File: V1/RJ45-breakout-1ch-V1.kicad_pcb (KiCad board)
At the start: 2 copper layers, 22.9 x 30.5 mm, 3 parts, among them J1 RJ45, J2 Screw_Terminal_01x04

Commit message: Footprint updated
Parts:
- removed REF**: OSHW-Logo2_7.3x6mm_Copper, Symbol:OSHW-Logo2_7.3x6mm_Copper

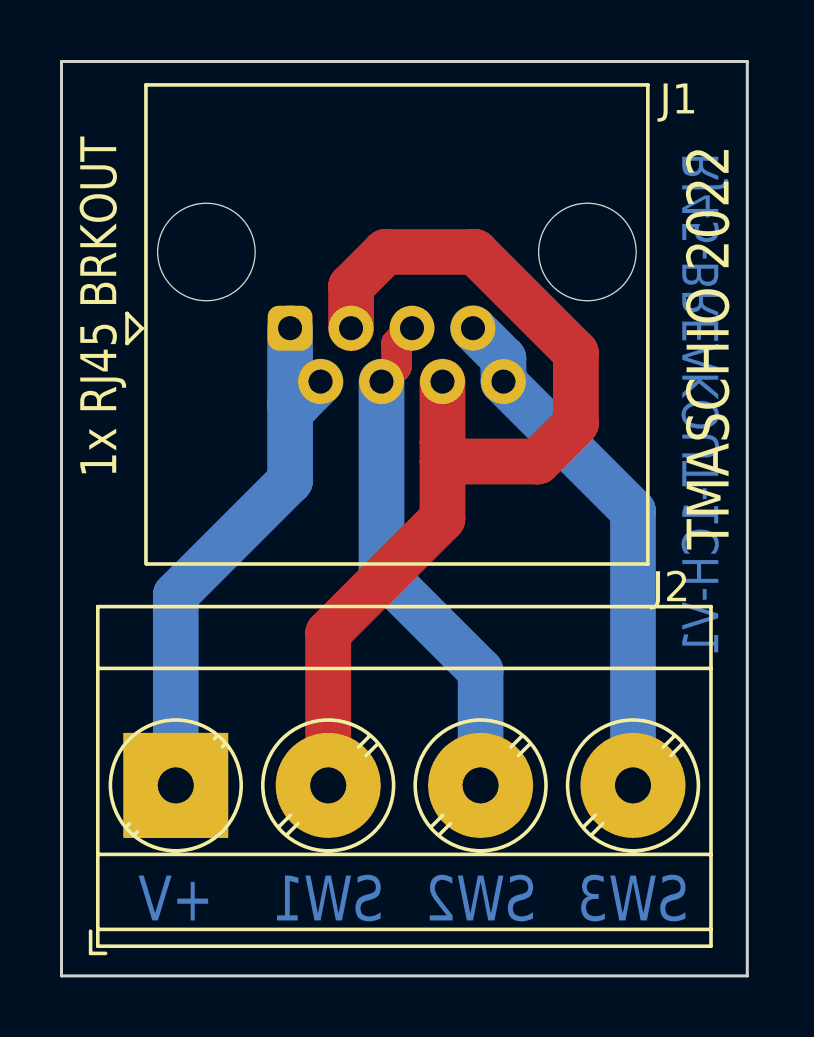
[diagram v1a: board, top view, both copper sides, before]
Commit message: PCB size optimization
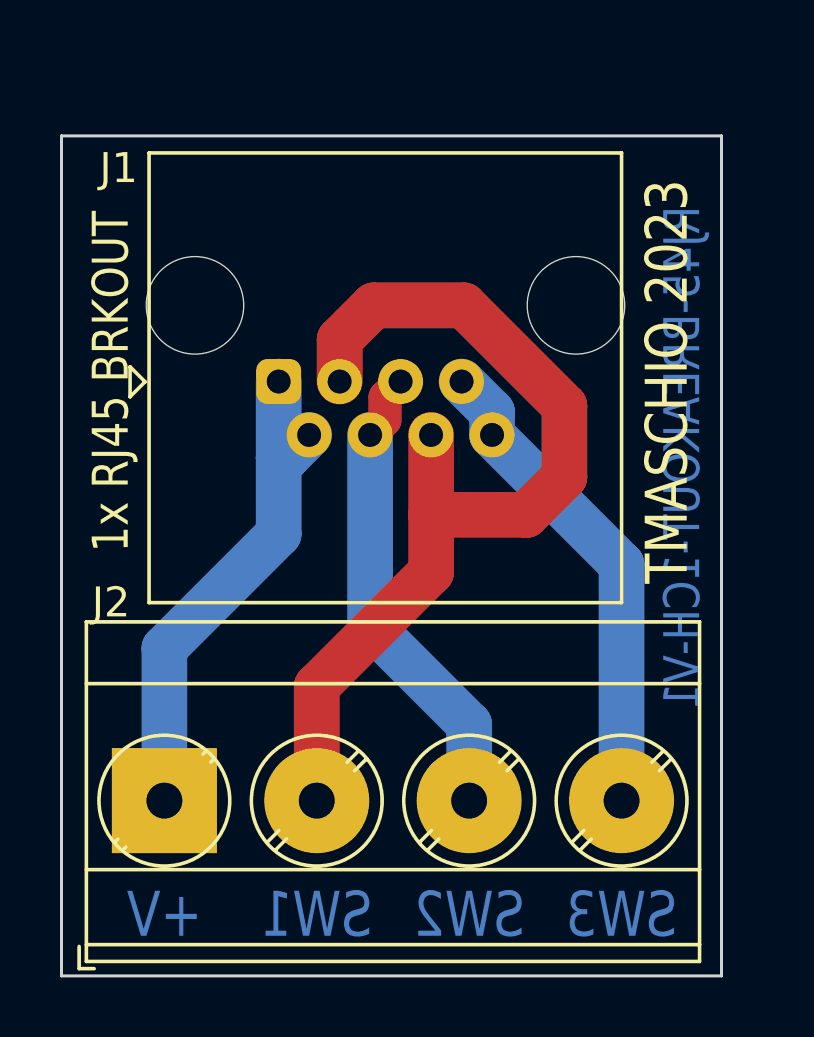
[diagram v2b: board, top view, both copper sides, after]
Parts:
- J2: value Screw_Terminal_01x04 -> SWITCHES
- moved J1 1.82 mm to (144.4, 94.5)
- moved J2 0.63 mm to (140.6, 108.5)
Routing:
- net Net-(J2-Pin_1): track 18.1 -> 16.9 mm
- net Net-(J2-Pin_4): track 17.4 -> 16.2 mm
- net Net-(J2-Pin_3): track 19.2 -> 18.0 mm
- net Net-(J2-Pin_2): track 33.1 -> 31.9 mm
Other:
- board size 22.9 x 30.5 mm -> 22 x 28 mm
- board text added: "TMASCHIO 2023"
- board text removed: "TMASCHIO 2022"

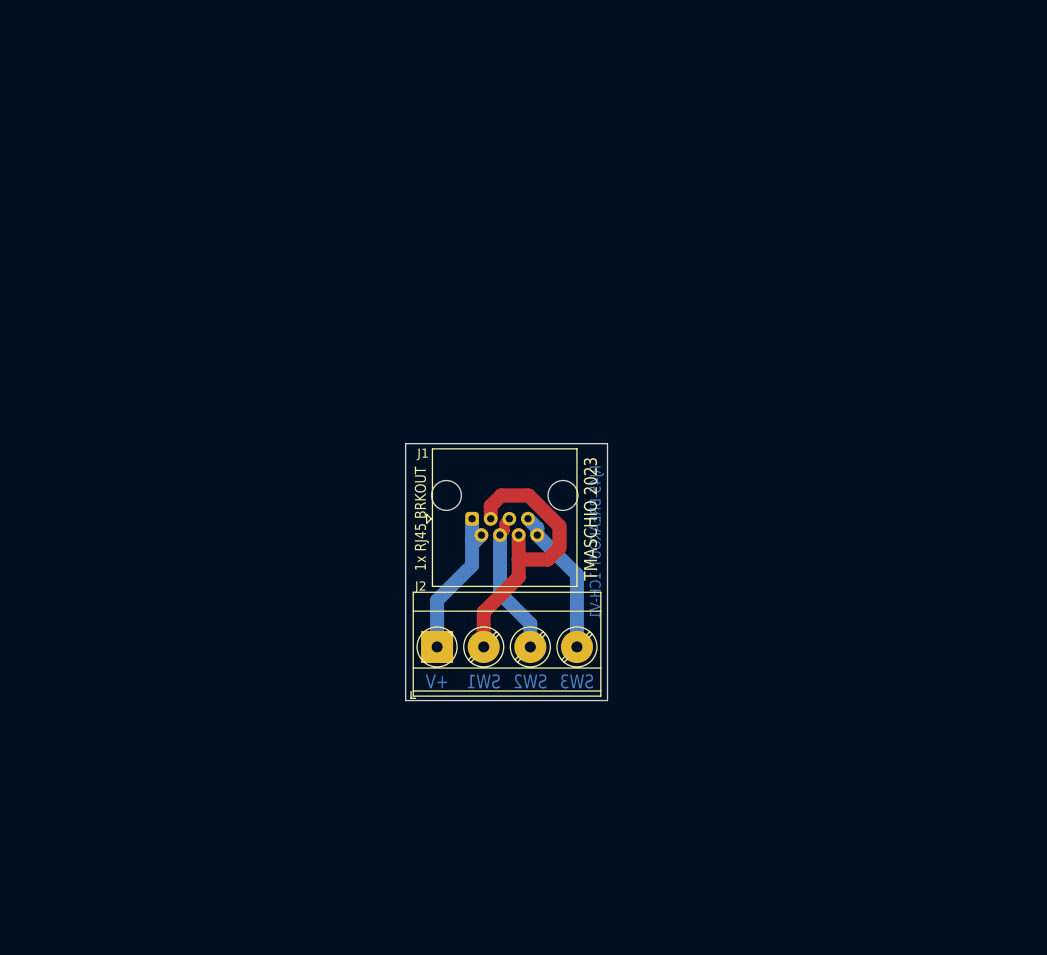
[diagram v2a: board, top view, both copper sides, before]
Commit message: Panelization
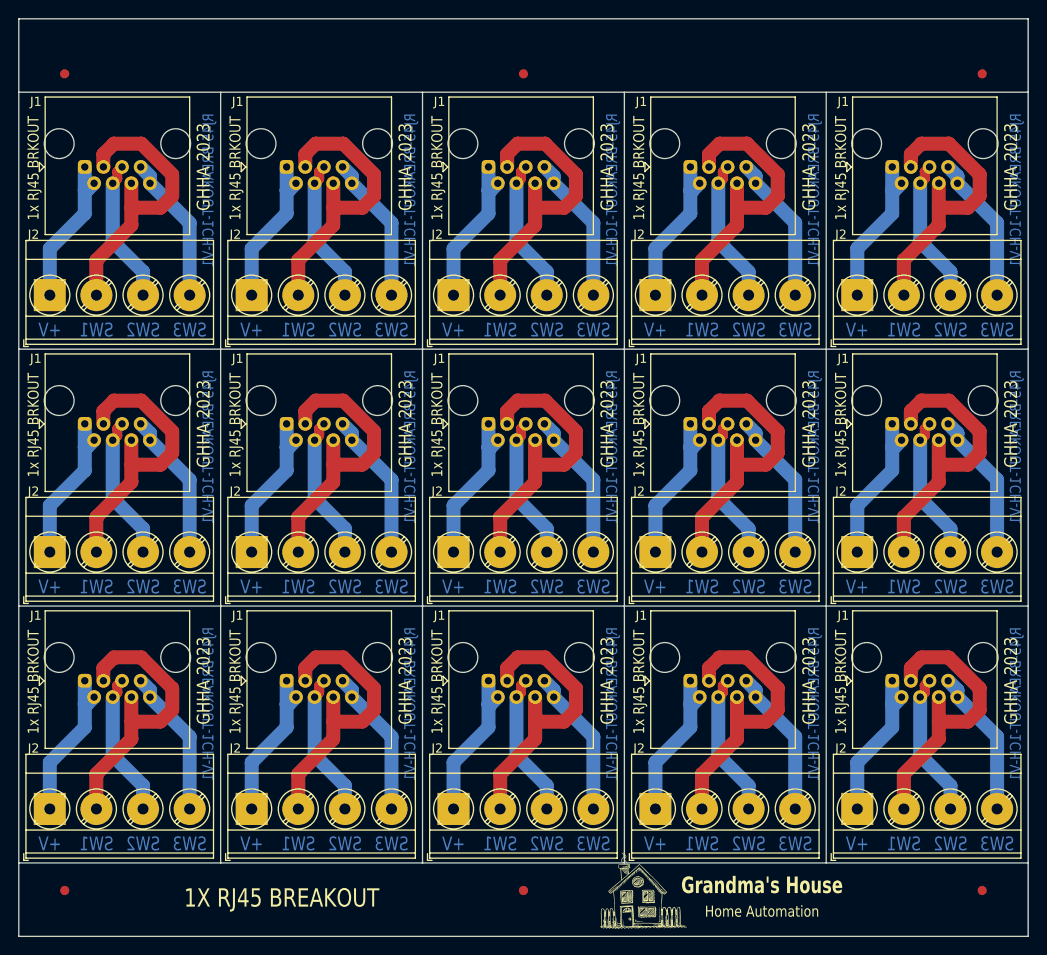
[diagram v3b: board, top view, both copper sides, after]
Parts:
- added ?: , Tales:Grandmas_small, F.Cu at (163.0, 135.0)
- added FID1: Fiducial_1mm_Mask2mm, Fiducial:Fiducial_1mm_Mask2mm, F.Cu at (100.0, 46.0)
- added FID2: Fiducial_1mm_Mask2mm, Fiducial:Fiducial_1mm_Mask2mm, F.Cu at (150.0, 46.0)
- added FID3: Fiducial_1mm_Mask2mm, Fiducial:Fiducial_1mm_Mask2mm, F.Cu at (200.0, 46.0)
- added FID4: Fiducial_1mm_Mask2mm, Fiducial:Fiducial_1mm_Mask2mm, F.Cu at (100.0, 135.0)
- added FID5: Fiducial_1mm_Mask2mm, Fiducial:Fiducial_1mm_Mask2mm, F.Cu at (150.0, 135.0)
- added FID6: Fiducial_1mm_Mask2mm, Fiducial:Fiducial_1mm_Mask2mm, F.Cu at (200.0, 135.0)
- added J1: RJ45, Tales:RJ45_Amphenol_RJHSE5080, F.Cu at (146.2, 84.1)
- added J1: RJ45, Tales:RJ45_Amphenol_RJHSE5080, F.Cu at (124.2, 112.1)
- added J1: RJ45, Tales:RJ45_Amphenol_RJHSE5080, F.Cu at (102.2, 56.1)
- added J1: RJ45, Tales:RJ45_Amphenol_RJHSE5080, F.Cu at (124.2, 84.1)
- added J1: RJ45, Tales:RJ45_Amphenol_RJHSE5080, F.Cu at (168.2, 56.1)
- added J1: RJ45, Tales:RJ45_Amphenol_RJHSE5080, F.Cu at (190.2, 112.1)
- added J1: RJ45, Tales:RJ45_Amphenol_RJHSE5080, F.Cu at (190.2, 56.1)
- added J1: RJ45, Tales:RJ45_Amphenol_RJHSE5080, F.Cu at (146.2, 56.1)
- added J1: RJ45, Tales:RJ45_Amphenol_RJHSE5080, F.Cu at (190.2, 84.1)
- added J1: RJ45, Tales:RJ45_Amphenol_RJHSE5080, F.Cu at (102.2, 84.1)
- added J1: RJ45, Tales:RJ45_Amphenol_RJHSE5080, F.Cu at (168.2, 112.1)
- added J1: RJ45, Tales:RJ45_Amphenol_RJHSE5080, F.Cu at (168.2, 84.1)
- added J1: RJ45, Tales:RJ45_Amphenol_RJHSE5080, F.Cu at (146.2, 112.1)
- added J1: RJ45, Tales:RJ45_Amphenol_RJHSE5080, F.Cu at (124.2, 56.1)
- added J2: SWITCHES, Tales:TerminalBlock_Phoenix_MKDS-3-4-5.08_1x04_P5.08mm_Horizontal, F.Cu at (186.4, 126.1)
- added J2: SWITCHES, Tales:TerminalBlock_Phoenix_MKDS-3-4-5.08_1x04_P5.08mm_Horizontal, F.Cu at (164.4, 70.1)
- added J2: SWITCHES, Tales:TerminalBlock_Phoenix_MKDS-3-4-5.08_1x04_P5.08mm_Horizontal, F.Cu at (164.4, 126.1)
- added J2: SWITCHES, Tales:TerminalBlock_Phoenix_MKDS-3-4-5.08_1x04_P5.08mm_Horizontal, F.Cu at (98.4, 98.1)
- added J2: SWITCHES, Tales:TerminalBlock_Phoenix_MKDS-3-4-5.08_1x04_P5.08mm_Horizontal, F.Cu at (186.4, 70.1)
- added J2: SWITCHES, Tales:TerminalBlock_Phoenix_MKDS-3-4-5.08_1x04_P5.08mm_Horizontal, F.Cu at (186.4, 98.1)
- added J2: SWITCHES, Tales:TerminalBlock_Phoenix_MKDS-3-4-5.08_1x04_P5.08mm_Horizontal, F.Cu at (98.4, 70.1)
- added J2: SWITCHES, Tales:TerminalBlock_Phoenix_MKDS-3-4-5.08_1x04_P5.08mm_Horizontal, F.Cu at (142.4, 126.1)
- added J2: SWITCHES, Tales:TerminalBlock_Phoenix_MKDS-3-4-5.08_1x04_P5.08mm_Horizontal, F.Cu at (164.4, 98.1)
- added J2: SWITCHES, Tales:TerminalBlock_Phoenix_MKDS-3-4-5.08_1x04_P5.08mm_Horizontal, F.Cu at (120.4, 126.1)
- added J2: SWITCHES, Tales:TerminalBlock_Phoenix_MKDS-3-4-5.08_1x04_P5.08mm_Horizontal, F.Cu at (142.4, 70.1)
- added J2: SWITCHES, Tales:TerminalBlock_Phoenix_MKDS-3-4-5.08_1x04_P5.08mm_Horizontal, F.Cu at (142.4, 98.1)
- added J2: SWITCHES, Tales:TerminalBlock_Phoenix_MKDS-3-4-5.08_1x04_P5.08mm_Horizontal, F.Cu at (120.4, 98.1)
- added J2: SWITCHES, Tales:TerminalBlock_Phoenix_MKDS-3-4-5.08_1x04_P5.08mm_Horizontal, F.Cu at (120.4, 70.1)
- moved J1 45.8 mm to (102.2, 112.1)
- moved J2 45.8 mm to (98.4, 126.1)
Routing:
- net Net-(J2-Pin_2): track 31.9 -> 477.8 mm
- net Net-(J2-Pin_3): track 18.0 -> 269.4 mm
- net Net-(J2-Pin_1): track 16.9 -> 253.2 mm
- net Net-(J2-Pin_4): track 16.2 -> 242.7 mm
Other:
- board size 22 x 28 mm -> 110 x 100 mm
- board text added: "1X RJ45 BREAKOUT"
- board text added: "GHHA 2023"
- board text added: "Grandma's House"
- board text added: "Home Automation"
- board text removed: "TMASCHIO 2023"
